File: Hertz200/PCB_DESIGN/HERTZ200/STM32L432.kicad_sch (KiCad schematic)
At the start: 18 parts, among them IC2 TMP108AIYFFT, J6 GPIO_PINS, J7 SWD_PINS, U1 STM32L431CCUx

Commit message: ROUTE DONE
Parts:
- removed IC2: TMP108AIYFFT, TMP108:TMP108AIYFFT, symbol TMP108AIYFFT:TMP108AIYFFT
- added IC2: TMP451HQDQWTQ1, Tmp451:SON50P250X200X80-8N, symbol TMP451HQDQWTQ1:TMP451HQDQWTQ1
- R29, R30: value 5K -> 10K
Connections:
- net +3V3: now also IC2.1 (V+)
- net GND: now also IC2.2 (D+), IC2.3 (D-), IC2.5 (GND)
- net TMP108_SCL renamed TMP451_SCL
- net TMP451_SCL: now also IC2.8 (SCL)
- net TMP108_SDA renamed TMP451_SDA
- net TMP451_SDA: now also IC2.7 (SDA)
- no-connect marks 12 -> 13
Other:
- moved on the sheet: R29, R30

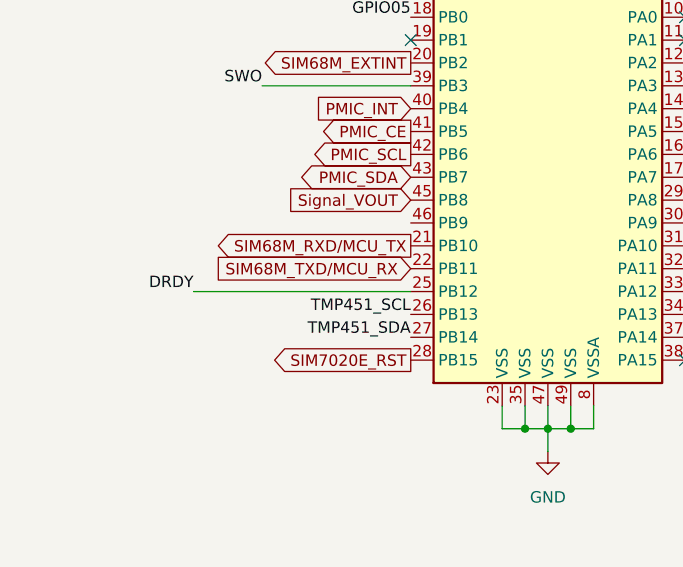
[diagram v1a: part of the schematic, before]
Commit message: Finished Schematics Review
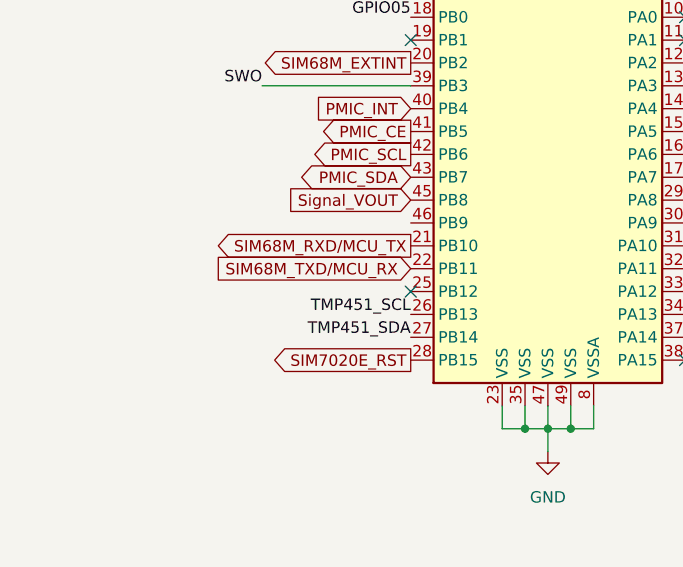
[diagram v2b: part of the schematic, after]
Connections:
- net DRDY: no longer names the net of U1.25 (PB12)
- no-connect marks 13 -> 14
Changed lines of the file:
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@@
   )
   (no_connect (at 119.38 88.9))
+  (no_connect (at 119.38 116.84))
   (no_connect (at 119.38 71.12))
   (no_connect (at 129.54 55.88))
@@
     (stroke (width 0) (type default) (color 0 0 0 0))
   )
-  (wire (pts (xy 95.25 116.84) (xy 119.38 116.84))
-    (stroke (width 0) (type default) (color 0 0 0 0))
-  )
   (wire (pts (xy 139.7 132.08) (xy 139.7 129.54))
     (stroke (width 0) (type default) (color 0 0 0 0))
@@
     (effects (font (size 1.27 1.27)) (justify right bottom))
   )
-  (label "DRDY" (at 95.25 116.84 180)
-    (effects (font (size 1.27 1.27)) (justify right bottom))
-  )

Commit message: BOM
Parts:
- removed J6: GPIO_PINS, Connector_PinHeader_2.54mm:PinHeader_1x07_P2.54mm_Vertical, symbol Connector:Conn_01x07_Male
- added J4: GPIO_PINS, Connector_PinHeader_2.54mm:PinHeader_1x06_P2.54mm_Vertical, symbol Connector:Conn_01x06_Male
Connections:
- net +3V3: now also J4.2 (Pin_2)
- net GND: now also J4.1 (Pin_1)
- net GPIO01: now also J4.3 (Pin_3)
- net GPIO02: now also J4.4 (Pin_4)
- net GPIO03: now also J4.5 (Pin_5)
- net GPIO05: now also J4.6 (Pin_6)
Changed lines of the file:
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@@
-    (stroke (width 0) (type default) (color 0 0 0 0))
-  )
-  (wire (pts (xy 127 184.15) (xy 124.46 184.15))
     (stroke (width 0) (type default) (color 0 0 0 0))
   )
@@
     (pin "2")
   )
-  (symbol (lib_id "Connector:Conn_01x07_Male") (at 119.38 176.53 0) (unit 1)
-    (in_bom yes) (on_board yes) (fields_autoplaced)
-    (property "Reference" "J6" (id 0) (at 120.015 163.83 0))
+  (symbol (lib_id "Connector:Conn_01x06_Male") (at 119.38 173.99 0) (unit 1)
+    (in_bom yes) (on_board yes) (fields_autoplaced)
+    (property "Reference" "J4" (id 0) (at 120.015 163.83 0))
     (property "Value" "GPIO_PINS" (id 1) (at 120.015 166.37 0))
-    (property "Footprint" "Connector_PinHeader_2.54mm:PinHeader_1x07_P2.54mm_Vertical" (id 2) (at 119.38 176.53 0)
-      (effects (font (size 1.27 1.27)) hide)
-    )
-    (property "Datasheet" "~" (id 3) (at 119.38 176.53 0)
+    (property "Footprint" "Connector_PinHeader_2.54mm:PinHeader_1x06_P2.54mm_Vertical" (id 2) (at 119.38 173.99 0)
+      (effects (font (size 1.27 1.27)) hide)
+    )
+    (property "Datasheet" "~" (id 3) (at 119.38 173.99 0)
       (effects (font (size 1.27 1.27)) hide)
     )
@@
     (pin "5")
     (pin "6")
-    (pin "7")
   )
   (symbol (lib_id "Device:C_Small") (at 237.49 60.96 0) (unit 1)
@@
     (pin "2")
   )
-  (symbol (lib_id "power:GND") (at 127 184.15 90) (unit 1)
-    (in_bom yes) (on_board yes) (fields_autoplaced)
-    (property "Reference" "#PWR0109" (id 0) (at 133.35 184.15 0)
-      (effects (font (size 1.27 1.27)) hide)
-    )
-    (property "Value" "GND" (id 1) (at 130.81 184.1499 90)
-      (effects (font (size 1.27 1.27)) (justify right))
-    )
-    (property "Footprint" "" (id 2) (at 127 184.15 0)
-      (effects (font (size 1.27 1.27)) hide)
-    )
-    (property "Datasheet" "" (id 3) (at 127 184.15 0)
-      (effects (font (size 1.27 1.27)) hide)
-    )
-    (pin "1")
-  )
   (symbol (lib_id "power:+3.3V") (at 208.28 118.11 0) (unit 1)

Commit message: update
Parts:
- removed R1: 0R, Resistor_SMD:R_0603_1608Metric, symbol Device:R_Small
- added C49, C50: 27pF, Capacitor_SMD:C_0603_1608Metric, symbol Device:C_Small
- added FB1: MPZ1608S471ATA00, Inductor_SMD:L_0603_1608Metric, symbol Device:FerriteBead_Small
- added R52: 10K, Resistor_SMD:R_0603_1608Metric, symbol Device:R_Small
- added Y1: ABM3B, ABM3B-8:XTAL_ABM3B-8.000MHZ-B2-T, symbol ABM3B-8.000MHZ-B2-T:ABM3B-8.000MHZ-B2-T
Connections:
- net +3V3: now also FB1.1
- net GND: now also C49.1, C50.1, R52.1, Y1.2 (GND), Y1.4 (GND)
- net VDDA: now also FB1.2
- net at U1.44 (PH3): now also R52.2
- net at U1.5 (PH0): now also C49.2, Y1.1
- net at U1.6 (PH1): now also C50.2, Y1.3
- net PMIC_CE: no longer names the net of U1.41 (PB5)
- net PMIC_INT: no longer names the net of U1.40 (PB4)
- net PMIC_SCL: no longer names the net of U1.42 (PB6)
- net PMIC_SDA: no longer names the net of U1.43 (PB7)
- net SIM7020E_RST: no longer names the net of U1.28 (PB15)
- no-connect marks 14 -> 16
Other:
- moved on the sheet: C1, S1
